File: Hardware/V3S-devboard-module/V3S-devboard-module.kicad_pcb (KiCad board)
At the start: 4 copper layers, 31.9 x 52.9 mm, 85 parts, among them CN1 AS0BC21-S30BE-7H, J201 Micro_SD_Card_Det1, J301 AS0BC21-S30BE-7H, SW201 SW_MEC_5E, U101 EA3036C, U102 XC6206PxxxMR, U201 V3S, U202 W25Q128JVS, Y201 Crystal_Small, Y202 Crystal_GND24_Small

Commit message: layout
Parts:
- removed SW201: SW_MEC_5E, v3s-devboard-module:SW_SKRPACE010
- R207: footprint Resistor_SMD:R_0603_1608Metric -> Resistor_SMD:R_0402_1005Metric
- moved C234 52.7 mm to (131.5, 87.6), turned to 90 degrees
- moved R207 52.3 mm to (133.1, 87.7)
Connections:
- C234 pad 2: /uP/RESET -> RESET
- J301 pad 10: unconnected-(J301-Pad10) -> ADCDAC.HPOUTR
- J301 pad 11: unconnected-(J301-Pad11) -> ADCDAC.HBIAS
- J301 pad 12: unconnected-(J301-Pad12) -> PB4_PWM0
- J301 pad 13: unconnected-(J301-Pad13) -> PB5_PWM1
- J301 pad 14: unconnected-(J301-Pad14) -> ETH_LED_SPD
- J301 pad 15: unconnected-(J301-Pad15) -> ETH_LED_LINK
- J301 pad 5: unconnected-(J301-Pad5) -> 5V
- J301 pad 6: unconnected-(J301-Pad6) -> RESET
- J301 pad 7: unconnected-(J301-Pad7) -> ADCDAC.HPCOM
- J301 pad 8: unconnected-(J301-Pad8) -> ADCDAC.HPCOMFB
- J301 pad 9: unconnected-(J301-Pad9) -> ADCDAC.HPOUTL
- R207 pad 2: /uP/RESET -> RESET
- U201 pad 99: /uP/RESET -> RESET
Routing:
- net RESET: track 0.00 -> 57.3 mm, vias 0 -> 2
- net 3V3: track 179.7 -> 166.2 mm, vias 25 -> 26
- net /uP/RESET: track 6.46 -> 0.00 mm
- net GND: track 38.1 -> 41.3 mm, vias 39 -> 54
- net ADCDAC.HPCOM: track 67.8 -> 69.5 mm
- net ADCDAC.HBIAS: track 60.3 -> 62.0 mm
- net ADCDAC.HPOUTL: track 63.5 -> 65.0 mm
- net PB5_PWM1: track 19.4 -> 20.9 mm
- net ETH_LED_SPD: track 39.7 -> 41.2 mm
- net ADCDAC.HPOUTR: track 62.0 -> 63.5 mm
- net ETH_LED_LINK: track 38.7 -> 40.1 mm
- net PB4_PWM0: track 22.8 -> 24.2 mm
- net ADCDAC.HPCOMFB: track 67.6 -> 68.9 mm
- net ETH0.TX_N: track 46.3 -> 45.4 mm
- net ETH0.TX_P: track 47.1 -> 46.2 mm
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
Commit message: layout
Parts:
- removed R211, R212, R213, R214, R215: 10k, Resistor_SMD:R_0603_1608Metric
- added C7: 1n, Capacitor_SMD:C_0402_1005Metric, B.Cu at (148.4, 90.5)
- added R7: 10k, Resistor_SMD:R_0402_1005Metric, F.Cu at (153.5, 73.7)
- added R8: 0, Resistor_SMD:R_0402_1005Metric, F.Cu at (138.1, 89.5)
- added RN1: R_Pack04, Resistor_SMD:R_Array_Concave_4x0402, F.Cu at (153.5, 75.5)
- added SW1: SW_MEC_5E, v3s-devboard-module:SW_SKRPACE010, F.Cu at (138.1, 86.0)
- C234: value 1u -> 100n; footprint Capacitor_SMD:C_0603_1608Metric -> Capacitor_SMD:C_0402_1005Metric
- R210: footprint Resistor_SMD:R_0603_1608Metric -> Resistor_SMD:R_0402_1005Metric
- moved C234 13.5 mm to (144.7, 84.6), turned to 0 degrees
- moved R207 11.7 mm to (144.7, 85.6), turned to 0 degrees
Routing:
- net SPI.MISO: track 5.46 -> 49.9 mm, vias 1 -> 2
- net GND: track 41.3 -> 54.0 mm, vias 54 -> 53
- net 3V3: track 166.2 -> 174.3 mm, vias 26 -> 30
- net SDC0.D0: track 31.4 -> 38.1 mm
- net SDC0.D1: track 30.2 -> 36.6 mm
- net 1V8: track 56.0 -> 61.8 mm
- net SDC0.CMD: track 22.9 -> 25.7 mm
- net RESET: track 57.3 -> 59.8 mm
- net SDC0.D2: track 21.7 -> 24.1 mm
- net SDC0.D3: track 23.3 -> 25.8 mm
- net LRADC0: track 64.6 -> 65.7 mm

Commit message: layout
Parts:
- removed CN1: AS0BC21-S30BE-7H, v3s-devboard-module:CONN-SMD_AS0BC21-S30BE-7H
- added J1: Conn_01x02, Connector_PinHeader_2.54mm:PinHeader_1x02_P2.54mm_Vertical, F.Cu at (146.6, 64.8)
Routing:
- net 5V: track 12.0 -> 41.3 mm
- net 3V3: track 174.3 -> 178.6 mm, vias 30 -> 31
- net GND: track 54.0 -> 53.3 mm, vias 53 -> 54
- net 1V2: track 179.1 -> 179.8 mm
- net /uP/SD_DET: track 36.1 -> 36.7 mm

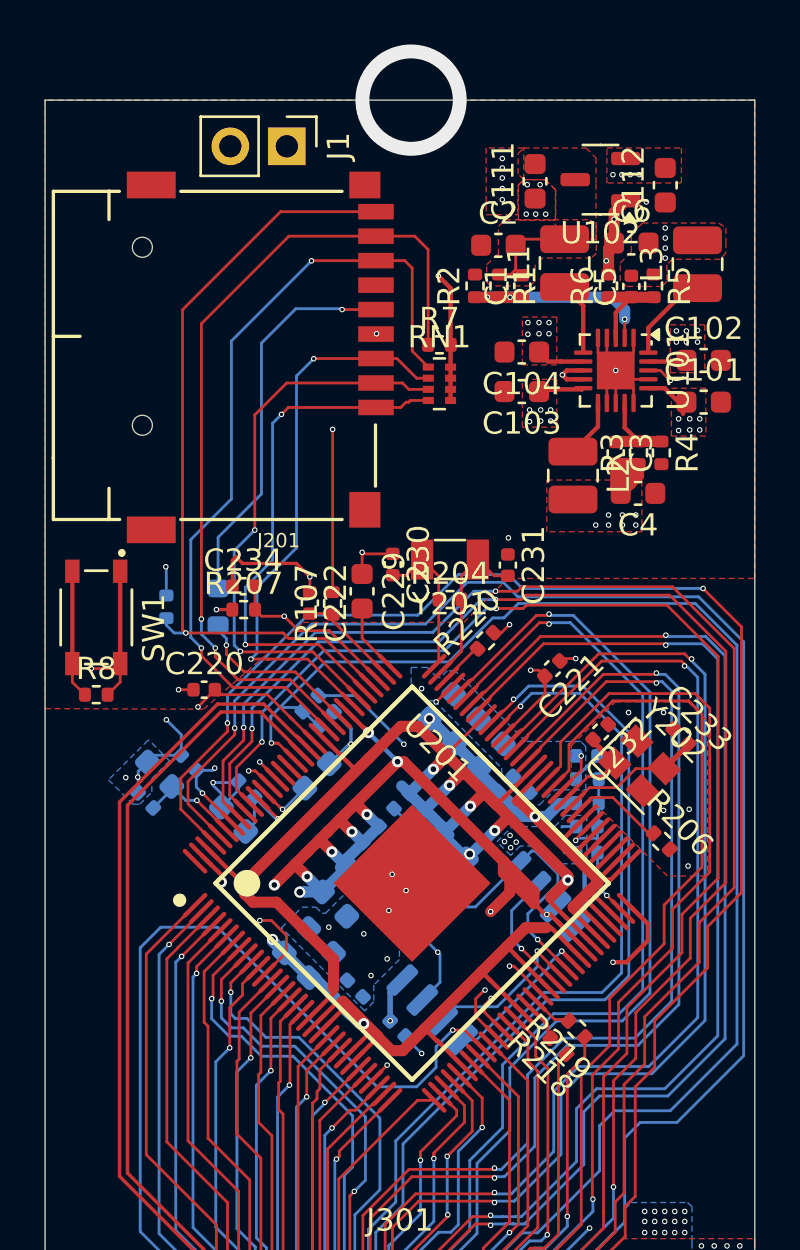
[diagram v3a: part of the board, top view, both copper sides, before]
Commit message: re-annotated everything
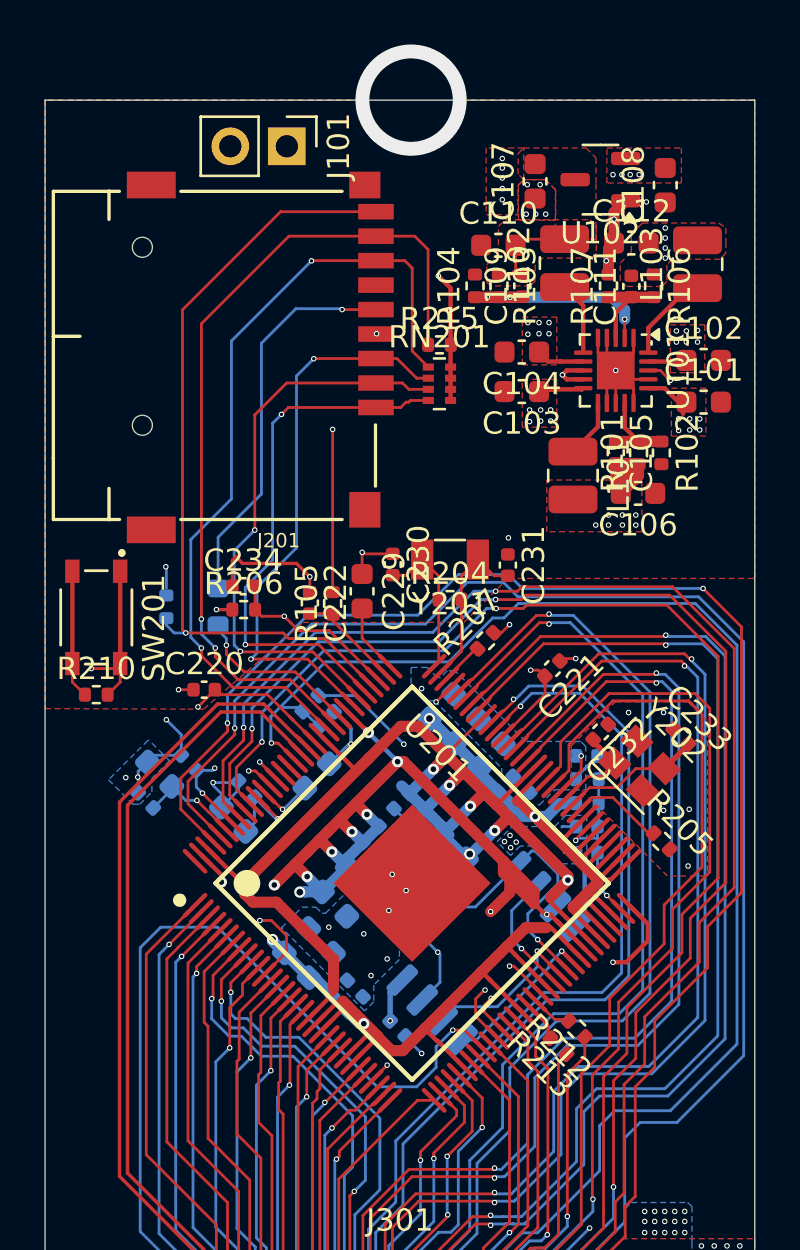
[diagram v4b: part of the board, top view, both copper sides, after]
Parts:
- renumbered C3 to C105, C4 to C106, C111 to C107, C112 to C108, C1 to C109, C2 to C110, C5 to C111, C6 to C112, C7 to C235, C235 to C236, J1 to J101, L2 to L101, L1 to L102, L3 to L103, R3 to R101, R4 to R102, R1 to R103, R2 to R104, R107 to R105, R5 to R106, R6 to R107, R206 to R205, R207 to R206, R220 to R207, R301 to R208, R208 to R209, R8 to R210, R209 to R211, R219 to R212, R218 to R213, R210 to R214, R7 to R215, RN1 to RN201, SW1 to SW201

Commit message: pre production tests
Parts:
- C235: value 1n -> 100n
- R207: footprint Resistor_SMD:R_0402_1005Metric -> Resistor_SMD:R_0805_2012Metric
- R211: footprint Resistor_SMD:R_0603_1608Metric -> Resistor_SMD:R_0402_1005Metric
- moved R207 0.63 mm to (155.7, 86.4)
- renumbered C107 to C106, C108 to C107, C109 to C108, C110 to C109, C111 to C110, C112 to C111, C106 to Ce101
